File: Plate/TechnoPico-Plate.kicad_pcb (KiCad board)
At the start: 2 copper layers, 139.1 x 77.2 mm, 4 parts

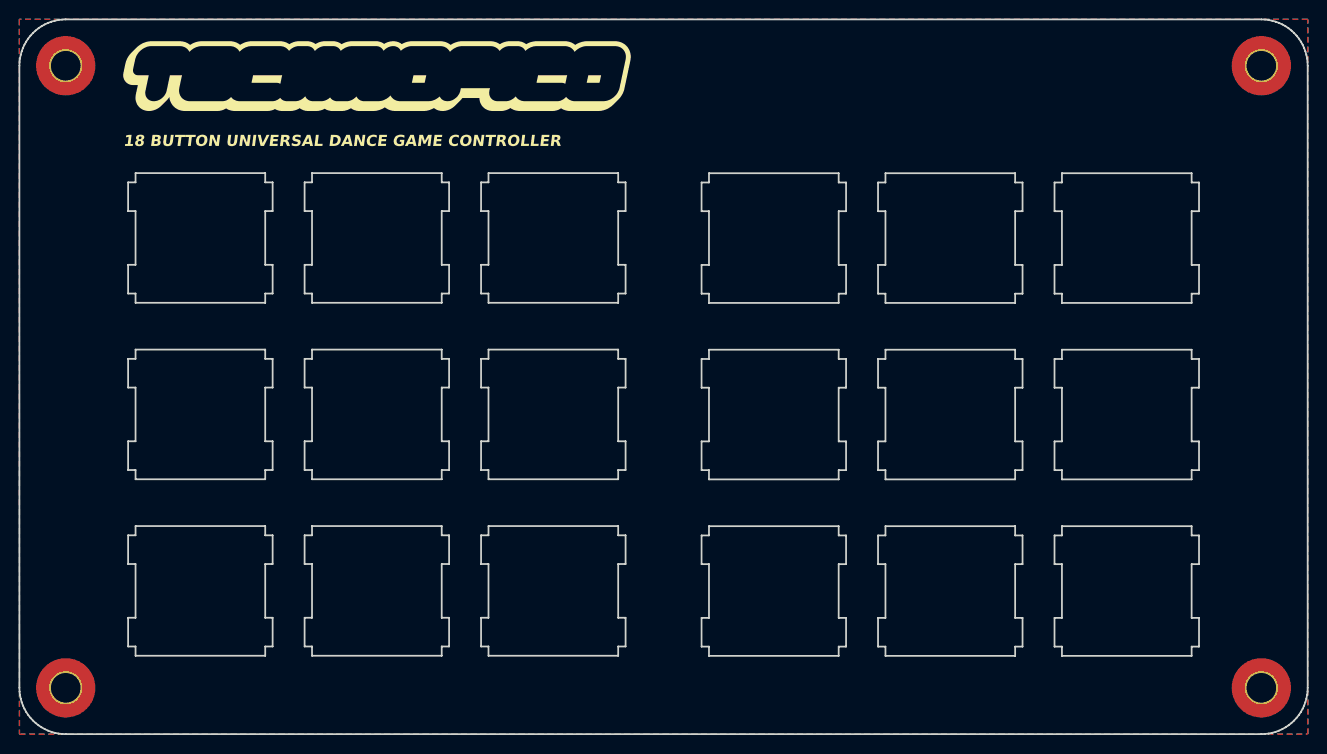
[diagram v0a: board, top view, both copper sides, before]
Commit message: Revert main PCB corner cutouts, add holes to plate
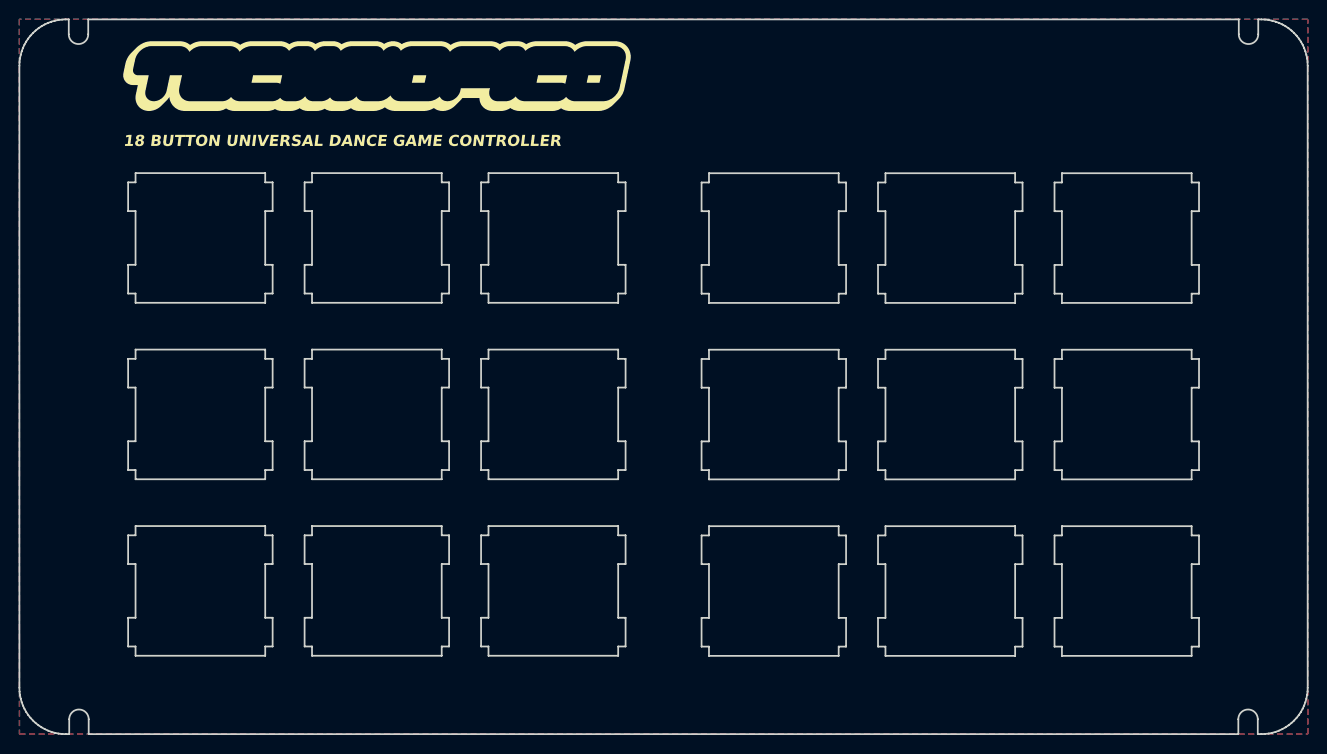
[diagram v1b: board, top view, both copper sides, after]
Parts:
- removed H1, H2, H3, H4: MountingHole_Pad_MP, MountingHole:MountingHole_3.2mm_M3_Pad_TopOnly
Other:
- outline, holes or cut-outs redrawn
